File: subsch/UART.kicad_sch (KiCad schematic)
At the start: 2 parts

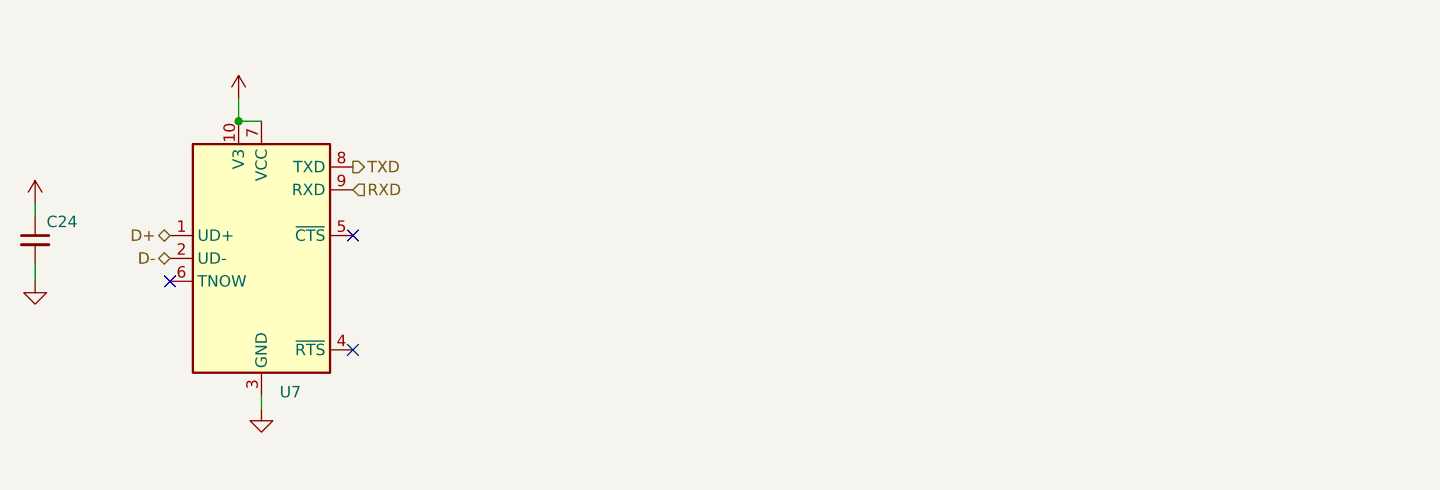
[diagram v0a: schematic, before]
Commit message: Big update on UART-pilot lamp/routings/connectors/esd protection
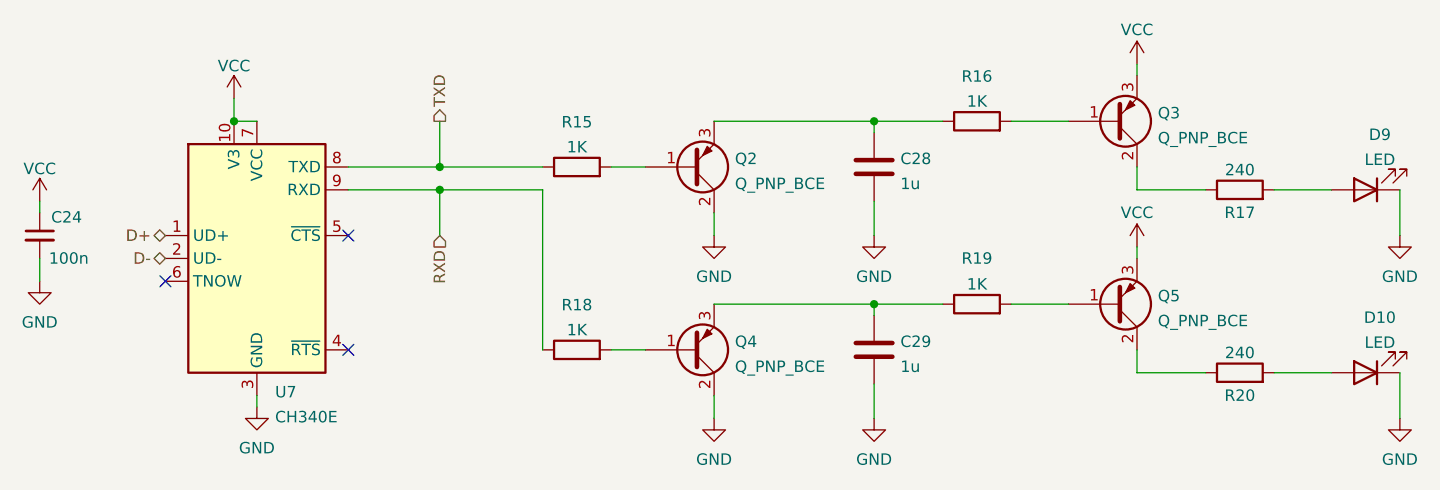
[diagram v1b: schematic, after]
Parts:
- added C28, C29: 1u, Capacitor_SMD:C_0603_1608Metric, symbol Device:C
- added D10, D9: LED, LED_SMD:LED_0603_1608Metric, symbol Device:LED
- added Q2, Q3, Q4, Q5: Q_PNP_BCE, Package_TO_SOT_SMD:SOT-23, symbol Device:Q_PNP_BCE
- added R15, R16, R18, R19: 1K, Resistor_SMD:R_0603_1608Metric, symbol Device:R
- added R17, R20: 240, Resistor_SMD:R_0603_1608Metric, symbol Device:R
- C24: value (none) -> 100n; footprint (none) -> Capacitor_SMD:C_0603_1608Metric
- U7: value (none) -> CH340E; footprint (none) -> Package_SO:MSOP-10_3x3mm_P0.5mm
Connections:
- net GND: now also C28.2, C29.2, D10.1 (K), D9.1 (K), Q2.2 (C), Q4.2 (C)
- net RXD: now also R18.1
- net TXD: now also R15.1
- net VCC: now also Q3.3 (E), Q5.3 (E)
- new net: C29.1, Q4.3 (E), R19.1
- new net: Q5.1 (B), R19.2
- new net: Q2.1 (B), R15.2
- new net: C28.1, Q2.3 (E), R16.1
- new net: Q3.1 (B), R16.2
- new net: Q4.1 (B), R18.2
- new net: Q3.2 (C), R17.1
- new net: D9.2 (A), R17.2
- new net: Q5.2 (C), R20.1
- new net: D10.2 (A), R20.2
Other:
- moved on the sheet: C24, U7
